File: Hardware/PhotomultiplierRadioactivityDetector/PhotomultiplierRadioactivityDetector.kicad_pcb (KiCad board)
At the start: 2 copper layers, 100 x 100 mm, 128 parts, among them J13 Conn_01x02_Female, J14 Conn_01x04, J15 Conn_02x05_Counter_Clockwise, Q1 2N7002, Q2 Q_NPN_BEC, Q3 Q_NMOS_GDS, U1 TL074, U2 TL074, U3 MCP3425A0T-ECH, U4 LM3488, U5 STM8S003F3P

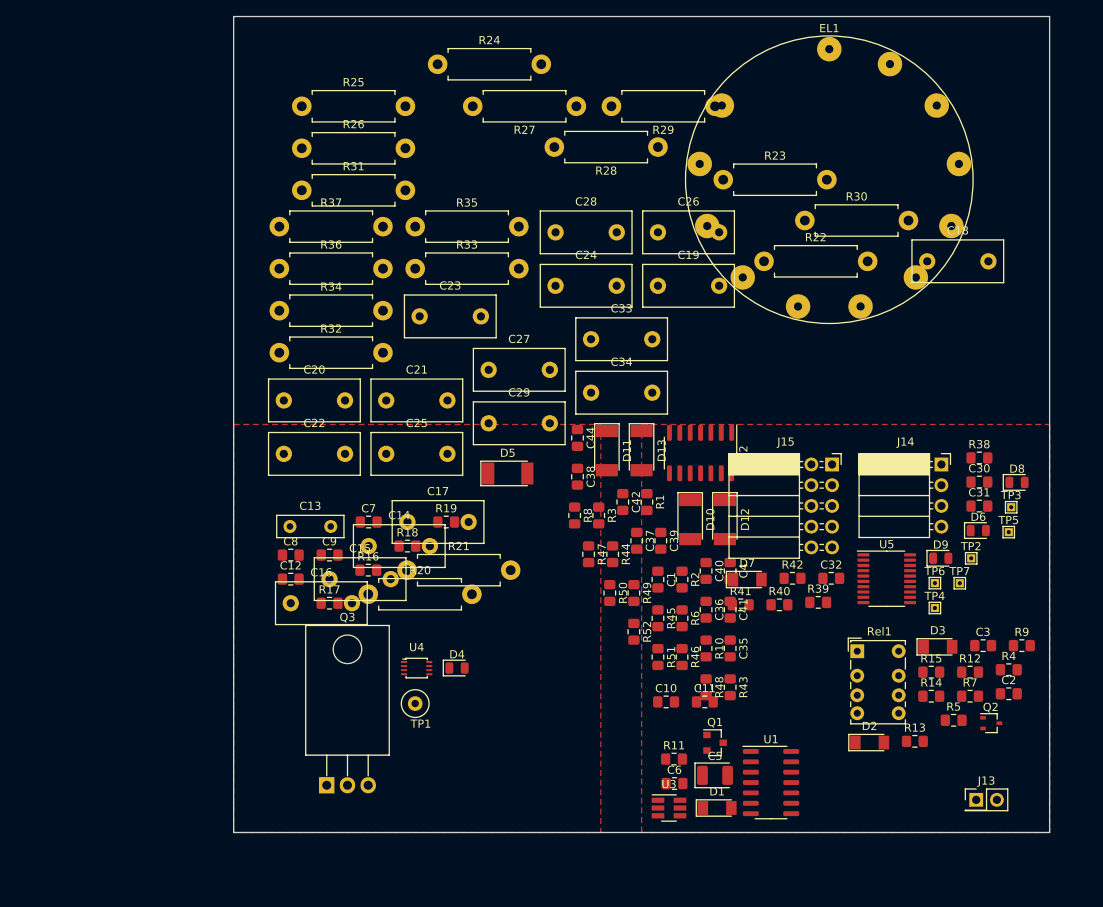
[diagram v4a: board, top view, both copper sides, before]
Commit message: reworked power supply for tube
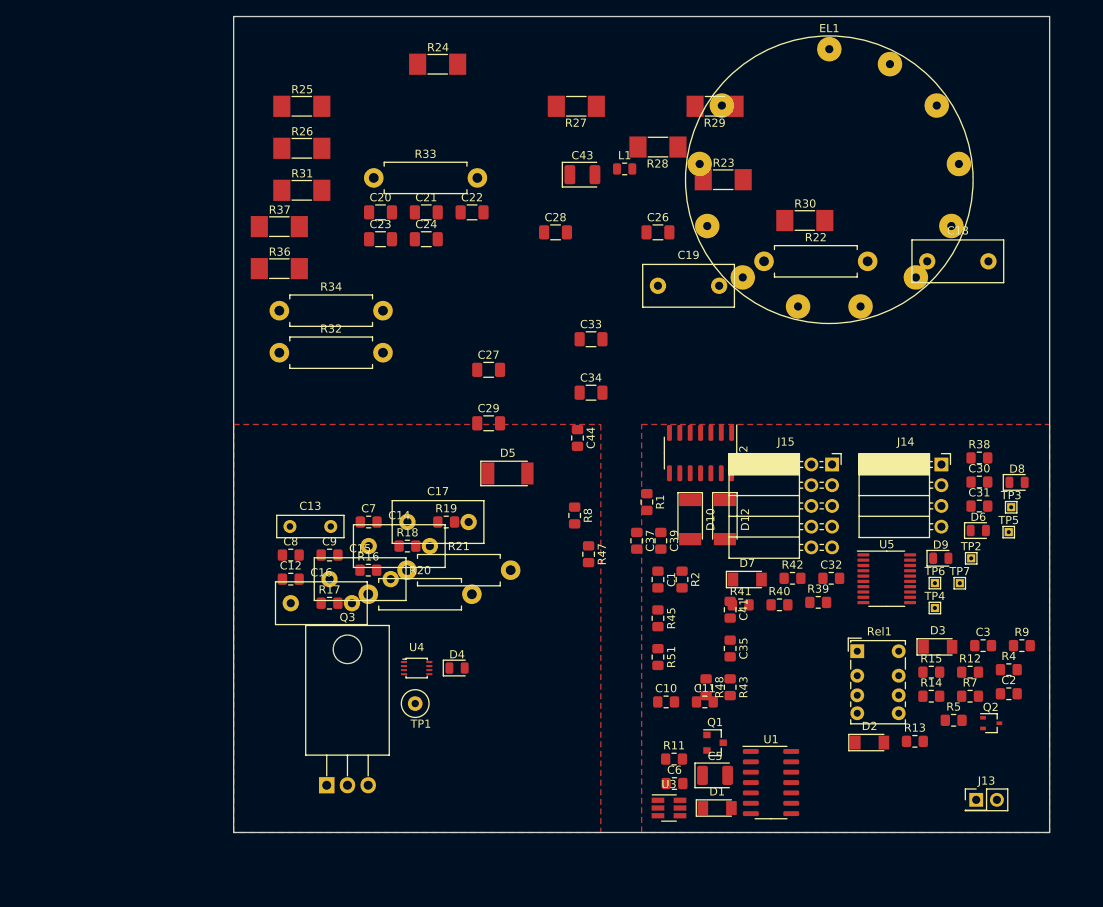
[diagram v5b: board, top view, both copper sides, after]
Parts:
- removed C25: 10n/3kV, Capacitor_THT:C_Disc_D11.0mm_W5.0mm_P7.50mm
- removed C36: 2p2, Capacitor_SMD:C_0805_2012Metric_Pad1.15x1.40mm_HandSolder
- removed C38: 1n, Capacitor_SMD:C_0805_2012Metric_Pad1.15x1.40mm_HandSolder
- removed C4, C40: 100n, Capacitor_SMD:C_0805_2012Metric_Pad1.15x1.40mm_HandSolder
- removed C42: 4p7+2p2, Capacitor_SMD:C_0805_2012Metric_Pad1.15x1.40mm_HandSolder
- removed D11, D13: 1n148, Diode_SMD:D_MELF
- removed R10: 0R, Resistor_SMD:R_0805_2012Metric_Pad1.15x1.40mm_HandSolder
- removed R3, R46, R49, R50, R6: 10k, Resistor_SMD:R_0805_2012Metric_Pad1.15x1.40mm_HandSolder
- removed R35: 150k, Resistor_THT:R_Axial_DIN0411_L9.9mm_D3.6mm_P12.70mm_Horizontal
- removed R44: 10G, Resistor_SMD:R_0805_2012Metric_Pad1.15x1.40mm_HandSolder
- removed R52: 10M, Resistor_SMD:R_0805_2012Metric_Pad1.15x1.40mm_HandSolder
- added C43: 1u/16V, Capacitor_Tantalum_SMD:CP_EIA-3528-21_Kemet-B, F.Cu at (67.7, 109.4)
- added L1: u68, Inductor_SMD:L_0805_2012Metric, F.Cu at (72.9, 108.7)
- C20, C21, C22, C23, C24, C26, C27, C28, C29, C33, C34: footprint Capacitor_THT:C_Disc_D11.0mm_W5.0mm_P7.50mm -> Capacitor_SMD:C_1206_3216Metric
- R23, R24, R25, R26, R27, R28, R31, R36, R37: value 150k -> 1M; footprint Resistor_THT:R_Axial_DIN0411_L9.9mm_D3.6mm_P12.70mm_Horizontal -> Resistor_SMD:R_MELF_MMB-0207
- R29: footprint Resistor_THT:R_Axial_DIN0411_L9.9mm_D3.6mm_P12.70mm_Horizontal -> Resistor_SMD:R_MELF_MMB-0207
- R30: value R -> 1M; footprint Resistor_THT:R_Axial_DIN0411_L9.9mm_D3.6mm_P12.70mm_Horizontal -> Resistor_SMD:R_MELF_MMB-0207
- moved C22 37.5 mm to (54.2, 114.0)
- moved C20 25.9 mm to (43.0, 114.0)
- moved C21 23.6 mm to (48.6, 114.0)
- moved C24 16.8 mm to (48.6, 117.3)
- moved R33 12.2 mm to (42.2, 109.8)
- moved C23 10.6 mm to (43.0, 117.3)
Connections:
- C20 pad 2: DYNOE_OUTPUT -> Net-(C20-Pad2)
- C21 pad 2: Net-(C18-Pad2) -> Net-(C21-Pad2)
- C22 pad 2: Net-(C21-Pad1) -> Net-(C22-Pad2)
- C23 pad 2: Net-(C22-Pad1) -> Net-(C23-Pad2)
- C24 pad 2: Net-(C23-Pad1) -> Net-(C24-Pad2)
- C26 pad 1: Net-(C26-Pad1) -> Net-(C20-Pad2)
- C27 pad 1: Net-(C27-Pad1) -> Net-(C21-Pad2)
- C27 pad 2: Net-(C26-Pad1) -> Net-(C20-Pad1)
- C28 pad 1: Net-(C28-Pad1) -> Net-(C22-Pad2)
- C28 pad 2: Net-(C27-Pad1) -> Net-(C21-Pad1)
- C29 pad 1: Net-(C29-Pad1) -> Net-(C23-Pad2)
- C29 pad 2: Net-(C28-Pad1) -> Net-(C22-Pad1)
- C33 pad 1: Net-(C33-Pad1) -> Net-(C24-Pad2)
- C33 pad 2: Net-(C29-Pad1) -> Net-(C23-Pad1)
- C34 pad 2: Net-(C33-Pad1) -> Net-(C24-Pad1)
- EL1 pad 10: Net-(C33-Pad1) -> Net-(C24-Pad2)
- EL1 pad 11: Net-(EL1-Pad11) -> Net-(C24-Pad1)
- EL1 pad 12: GND -> Net-(EL1-Pad12)
- EL1 pad 2: Net-(C26-Pad1) -> Net-(C20-Pad2)
- EL1 pad 3: Net-(C21-Pad1) -> Net-(C20-Pad1)
- EL1 pad 4: Net-(C27-Pad1) -> Net-(C21-Pad2)
- EL1 pad 5: Net-(C22-Pad1) -> Net-(C21-Pad1)
- EL1 pad 6: Net-(C28-Pad1) -> Net-(C22-Pad2)
- EL1 pad 7: Net-(C23-Pad1) -> Net-(C22-Pad1)
- EL1 pad 8: Net-(C29-Pad1) -> Net-(C23-Pad2)
- EL1 pad 9: Net-(C24-Pad1) -> Net-(C23-Pad1)
- R23 pad 1: Net-(C26-Pad1) -> Net-(C20-Pad2)
- R24 pad 1: Net-(C21-Pad1) -> Net-(C20-Pad1)
- R24 pad 2: Net-(C26-Pad1) -> Net-(C20-Pad2)
- R25 pad 1: Net-(C27-Pad1) -> Net-(C21-Pad2)
- R25 pad 2: Net-(C21-Pad1) -> Net-(C20-Pad1)
- R26 pad 1: Net-(C22-Pad1) -> Net-(C21-Pad1)
- R26 pad 2: Net-(C27-Pad1) -> Net-(C21-Pad2)
- R27 pad 1: Net-(C28-Pad1) -> Net-(C22-Pad2)
- R27 pad 2: Net-(C22-Pad1) -> Net-(C21-Pad1)
- R28 pad 1: Net-(C23-Pad1) -> Net-(C22-Pad1)
- R28 pad 2: Net-(C28-Pad1) -> Net-(C22-Pad2)
- R29 pad 1: Net-(C29-Pad1) -> Net-(C23-Pad2)
- R29 pad 2: Net-(C23-Pad1) -> Net-(C22-Pad1)
- R30 pad 1: Net-(C24-Pad1) -> Net-(C23-Pad1)
- R30 pad 2: Net-(C29-Pad1) -> Net-(C23-Pad2)
- R31 pad 1: Net-(C33-Pad1) -> Net-(C24-Pad2)
- R31 pad 2: Net-(C24-Pad1) -> Net-(C23-Pad1)
- R33 pad 1: DYNOE_OUTPUT -> GND
- R33 pad 2: GND -> Net-(EL1-Pad12)
- R34 pad 1: Net-(C18-Pad2) -> Net-(EL1-Pad12)
- R36 pad 1: Net-(EL1-Pad11) -> Net-(C24-Pad1)
- R36 pad 2: Net-(C33-Pad1) -> Net-(C24-Pad2)
- R37 pad 2: Net-(EL1-Pad11) -> Net-(C24-Pad1)
- U1 pad 10: Net-(C4-Pad1) -> (no net)
- U1 pad 12: Net-(C40-Pad1) -> (no net)
- U1 pad 13: Net-(C42-Pad2) -> (no net)
- U1 pad 14: Net-(C42-Pad1) -> (no net)
- U1 pad 8: Net-(C36-Pad1) -> (no net)
- U1 pad 9: DYNOE_OUTPUT -> (no net)

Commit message: placement of components for tube driver
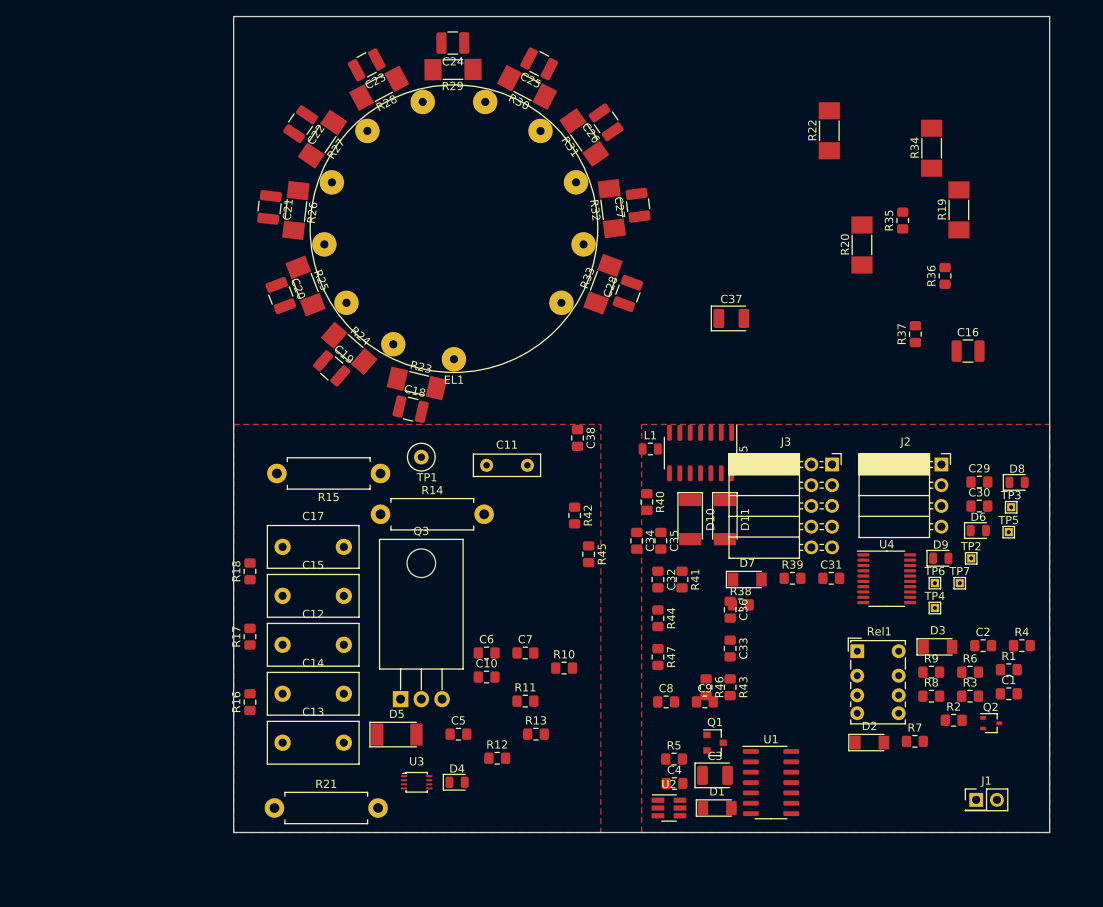
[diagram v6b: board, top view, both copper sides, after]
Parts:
- added R12: 10k, Resistor_SMD:R_0805_2012Metric_Pad1.15x1.40mm_HandSolder, F.Cu at (57.3, 180.9)
- added R16: 1k, Resistor_SMD:R_0805_2012Metric_Pad1.15x1.40mm_HandSolder, F.Cu at (27.0, 174.0)
- added R17: 1k, Resistor_SMD:R_0805_2012Metric_Pad1.15x1.40mm_HandSolder, F.Cu at (27.0, 166.0)
- added R19: 30k, Resistor_SMD:R_MELF_MMB-0207, F.Cu at (113.9, 113.7)
- C12: renamed from C14; value 10n -> 10n/2kV
- C13: renamed from C15; value 10n -> 10n/2kV
- C14: renamed from C16; value 10n -> 10n/2kV
- C15: renamed from C17; value 10n -> 10n/2kV
- C16: renamed from C19; footprint Capacitor_THT:C_Disc_D11.0mm_W5.0mm_P7.50mm -> Capacitor_SMD:C_1210_3225Metric
- C18: renamed from C26; footprint Capacitor_SMD:C_1206_3216Metric -> Capacitor_SMD:C_1210_3225Metric
- C19: renamed from C20; footprint Capacitor_SMD:C_1206_3216Metric -> Capacitor_SMD:C_1210_3225Metric
- C20: renamed from C27; footprint Capacitor_SMD:C_1206_3216Metric -> Capacitor_SMD:C_1210_3225Metric
- C21: footprint Capacitor_SMD:C_1206_3216Metric -> Capacitor_SMD:C_1210_3225Metric
- C22: renamed from C28; footprint Capacitor_SMD:C_1206_3216Metric -> Capacitor_SMD:C_1210_3225Metric
- C23: renamed from C22; footprint Capacitor_SMD:C_1206_3216Metric -> Capacitor_SMD:C_1210_3225Metric
- C24: renamed from C29; footprint Capacitor_SMD:C_1206_3216Metric -> Capacitor_SMD:C_1210_3225Metric
- C25: renamed from C23; footprint Capacitor_SMD:C_1206_3216Metric -> Capacitor_SMD:C_1210_3225Metric
- C26: renamed from C33; footprint Capacitor_SMD:C_1206_3216Metric -> Capacitor_SMD:C_1210_3225Metric
- C27: renamed from C24; footprint Capacitor_SMD:C_1206_3216Metric -> Capacitor_SMD:C_1210_3225Metric
- C28: renamed from C34; footprint Capacitor_SMD:C_1206_3216Metric -> Capacitor_SMD:C_1210_3225Metric
- R18: value 10k -> 1k
- R20: renamed from R32; footprint Resistor_THT:R_Axial_DIN0411_L9.9mm_D3.6mm_P12.70mm_Horizontal -> Resistor_SMD:R_MELF_MMB-0207
- R22: renamed from R34; footprint Resistor_THT:R_Axial_DIN0411_L9.9mm_D3.6mm_P12.70mm_Horizontal -> Resistor_SMD:R_MELF_MMB-0207
- R34: renamed from R33; footprint Resistor_THT:R_Axial_DIN0411_L9.9mm_D3.6mm_P12.70mm_Horizontal -> Resistor_SMD:R_MELF_MMB-0207
- moved R21 89.9 mm to (30.0, 187.0)
- moved C17 86.4 mm to (31.0, 155.0)
- moved R20 72.6 mm to (102.0, 118.0), turned to 90 degrees
- moved R22 70.9 mm to (98.0, 104.0), turned to 90 degrees
- moved R34 68.5 mm to (110.5, 106.1), turned to 90 degrees
- moved C24 46.8 mm to (51.9, 93.3), turned to 180.346 degrees
- moved EL1 46.4 mm to (52.0, 116.0), turned to 180 degrees
- moved R23 45.1 mm to (47.4, 135.0), turned to 346.5 degrees
- moved R36 42.9 mm to (112.2, 121.8), turned to 90 degrees
- moved R32 41.4 mm to (71.3, 113.5), turned to 97.2692 degrees
- moved R33 40.3 mm to (70.3, 122.8), turned to 69.5769 degrees
- moved C16 38.8 mm to (115.0, 131.0)
- moved R30 37.8 mm to (61.0, 98.7), turned to 152.654 degrees
- moved C18 37.3 mm to (46.7, 138.1), turned to 346.5 degrees
- moved R37 37.1 mm to (108.5, 128.9), turned to 90 degrees
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- renumbered C2 to C1, C12 to C10, C13 to C11, C18 to C17, C3 to C2, C30 to C29, C5 to C3, C31 to C30, C32 to C31, C1 to C32, C35 to C33, C37 to C34, C39 to C35, C41 to C36, C43 to C37, C44 to C38, C6 to C4, C7 to C5, C8 to C6, C9 to C7, C10 to C8, C11 to C9, D12 to D11, J13 to J1, J14 to J2, J15 to J3, R4 to R1, R16 to R10, R17 to R11, R19 to R13, R20 to R14, R21 to R15, R5 to R2, R22 to R21, R7 to R3, R36 to R32, R37 to R33, R38 to R35, R39 to R36, R40 to R37, R41 to R38, R42 to R39, R9 to R4, R1 to R40, R2 to R41, R8 to R42, R45 to R44, R47 to R45, R48 to R46, R51 to R47, R11 to R5, R12 to R6, R13 to R7, R14 to R8, R15 to R9, U3 to U2, U4 to U3, U5 to U4, U2 to U5
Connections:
- C12 pad 2: Net-(C14-Pad2) -> Net-(C12-Pad2)
- C13 pad 2: Net-(C14-Pad2) -> Net-(C13-Pad2)
- C15 pad 2: Net-(C14-Pad2) -> Net-(C15-Pad2)
- D5 pad 1: Net-(C14-Pad2) -> Net-(C12-Pad2)
- R14 pad 1: Net-(C14-Pad2) -> Net-(C12-Pad2)
- R18 pad 1: Net-(R18-Pad1) -> Net-(C15-Pad2)
- R18 pad 2: GND -> Net-(C14-Pad2)
- TP1 pad 1: Net-(C14-Pad2) -> Net-(R19-Pad1)
- U3 pad 7: Net-(R18-Pad1) -> Net-(R12-Pad1)

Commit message: add element,, footprint and 3d model for transformer
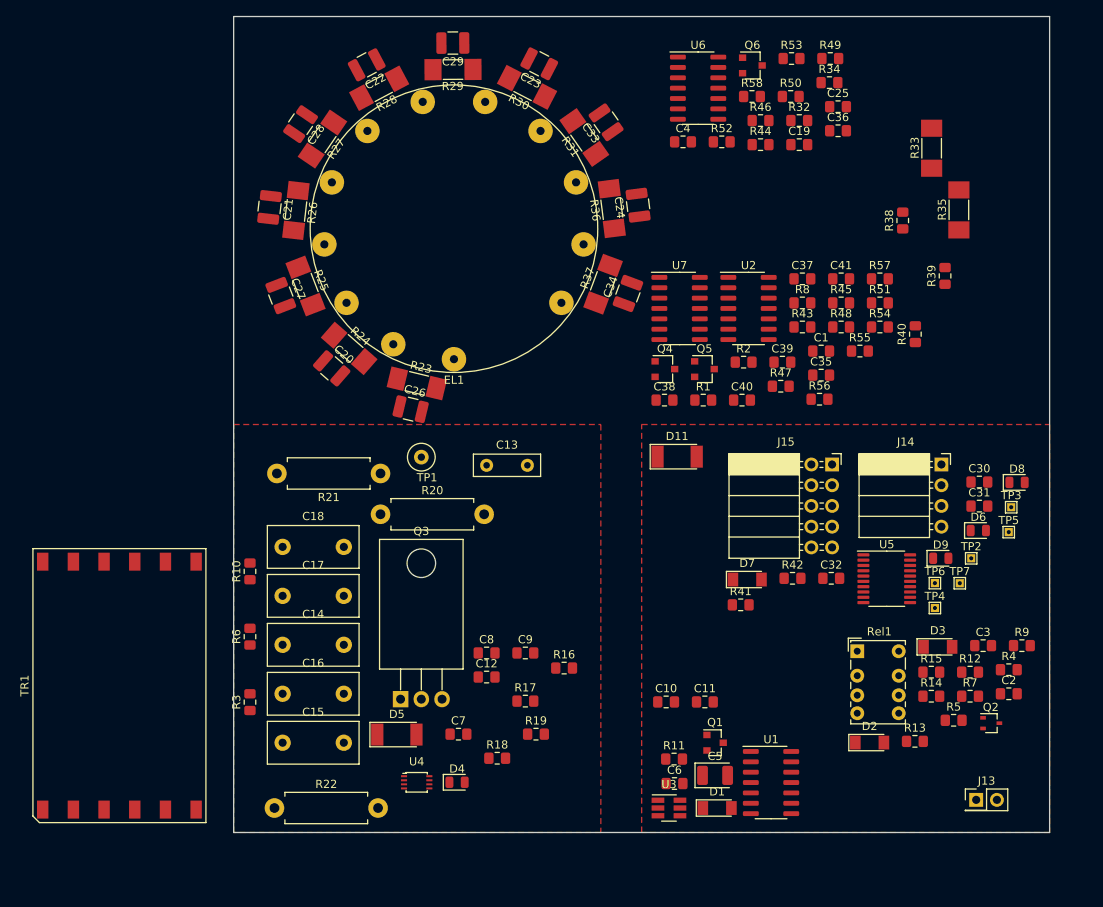
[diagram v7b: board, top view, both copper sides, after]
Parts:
- removed the C16 at (115.0, 131.0)
- removed the C32 at (77.0, 159.0)
- removed the C33 at (85.8, 167.4)
- removed the C34 at (74.4, 154.2)
- removed D10: 1n148, Diode_SMD:D_MELF
- removed L1: u68, Inductor_SMD:L_0805_2012Metric
- removed the R20 at (102.0, 118.0)
- removed the R22 at (98.0, 104.0)
- removed the R40 at (75.6, 149.5)
- removed the R41 at (80.0, 159.0)
- removed the R42 at (66.8, 151.2)
- removed the U5 at (82.2, 143.5)
- added C1: 100n, Capacitor_SMD:C_0805_2012Metric_Pad1.15x1.40mm_HandSolder, F.Cu at (97.0, 131.0)
- added C19: 2p2, Capacitor_SMD:C_0805_2012Metric_Pad1.15x1.40mm_HandSolder, F.Cu at (94.3, 105.7)
- added C25: 100n, Capacitor_SMD:C_0805_2012Metric_Pad1.15x1.40mm_HandSolder, F.Cu at (99.1, 101.0)
- added C39: 1n, Capacitor_SMD:C_0805_2012Metric_Pad1.15x1.40mm_HandSolder, F.Cu at (92.2, 132.4)
- added C4: 100n, Capacitor_SMD:C_0805_2012Metric_Pad1.15x1.40mm_HandSolder, F.Cu at (80.1, 105.4)
- added C40: 100n, Capacitor_SMD:C_0805_2012Metric_Pad1.15x1.40mm_HandSolder, F.Cu at (87.3, 137.0)
- added C41: 4p7+2p2, Capacitor_SMD:C_0805_2012Metric_Pad1.15x1.40mm_HandSolder, F.Cu at (99.5, 122.2)
- added Q4: Q_NJFET_DGS, Package_TO_SOT_SMD:SC-59, F.Cu at (77.8, 133.2)
- added Q5: Q_NJFET_DGS, Package_TO_SOT_SMD:SC-59, F.Cu at (82.7, 133.2)
- added Q6: Q_NJFET_DGS, Package_TO_SOT_SMD:SC-59, F.Cu at (88.6, 96.0)
- added R1: 470k, Resistor_SMD:R_0805_2012Metric_Pad1.15x1.40mm_HandSolder, F.Cu at (82.5, 137.0)
- added R2: 10k, Resistor_SMD:R_0805_2012Metric_Pad1.15x1.40mm_HandSolder, F.Cu at (87.5, 132.4)
- added R32: 10k, Resistor_SMD:R_0805_2012Metric_Pad1.15x1.40mm_HandSolder, F.Cu at (94.3, 102.8)
- added R34: 10k, Resistor_SMD:R_0805_2012Metric_Pad1.15x1.40mm_HandSolder, F.Cu at (98.0, 98.1)
- added R48: 10k, Resistor_SMD:R_0805_2012Metric_Pad1.15x1.40mm_HandSolder, F.Cu at (99.5, 128.1)
- added R49: 10k, Resistor_SMD:R_0805_2012Metric_Pad1.15x1.40mm_HandSolder, F.Cu at (98.1, 95.2)
- added R50: 10k, Resistor_SMD:R_0805_2012Metric_Pad1.15x1.40mm_HandSolder, F.Cu at (93.3, 99.8)
- added R51: 10k, Resistor_SMD:R_0805_2012Metric_Pad1.15x1.40mm_HandSolder, F.Cu at (104.2, 125.1)
- added R52: 10k, Resistor_SMD:R_0805_2012Metric_Pad1.15x1.40mm_HandSolder, F.Cu at (84.8, 105.4)
- added R53: 10M, Resistor_SMD:R_0805_2012Metric_Pad1.15x1.40mm_HandSolder, F.Cu at (93.4, 95.2)
- added R54: 10k, Resistor_SMD:R_0805_2012Metric_Pad1.15x1.40mm_HandSolder, F.Cu at (104.2, 128.1)
- added R55: 10k, Resistor_SMD:R_0805_2012Metric_Pad1.15x1.40mm_HandSolder, F.Cu at (101.8, 131.0)
- added R56: 10k, Resistor_SMD:R_0805_2012Metric_Pad1.15x1.40mm_HandSolder, F.Cu at (96.8, 136.9)
- added R57: 10M, Resistor_SMD:R_0805_2012Metric_Pad1.15x1.40mm_HandSolder, F.Cu at (104.2, 122.2)
- added R58: 10k, Resistor_SMD:R_0805_2012Metric_Pad1.15x1.40mm_HandSolder, F.Cu at (88.5, 99.8)
- added R8: 10k, Resistor_SMD:R_0805_2012Metric_Pad1.15x1.40mm_HandSolder, F.Cu at (94.7, 125.1)
- added TR1: 750311771, PhotomultiplierRadioactivityDetector:750311771, F.Cu at (11.0, 172.0)
- added U2: TL074, Package_SO:SOIC-14_3.9x8.7mm_P1.27mm, F.Cu at (88.1, 125.8)
- added U6: TL074, Package_SO:SOIC-14_3.9x8.7mm_P1.27mm, F.Cu at (81.9, 98.8)
- added U7: TL074, Package_SO:SOIC-14_3.9x8.7mm_P1.27mm, F.Cu at (79.7, 125.8)
- C35: value 100n -> 2p2
- C36: value 4p7+2p2 -> 10n
- C37: value 1u/16V -> 100n; footprint Capacitor_Tantalum_SMD:CP_EIA-3528-21_Kemet-B -> Capacitor_SMD:C_0805_2012Metric_Pad1.15x1.40mm_HandSolder
- R10: renamed from R18; value 1k -> 510R
- R3: renamed from R16; value 1k -> 510R
- R35: renamed from R19; value 30k -> 510R
- R43: value 10G -> 10k
- R44: value 10k -> 0R
- R46: value 10k -> 10G
- R47: value 10M -> 10k
- R6: renamed from R17; value 1k -> 510R
- moved R46 69.8 mm to (89.6, 102.8), turned to 0 degrees
- moved C36 60.2 mm to (99.1, 104.0), turned to 0 degrees
- moved R44 59.4 mm to (89.6, 105.7), turned to 0 degrees
- moved R43 45.0 mm to (94.7, 128.1), turned to 0 degrees
- moved R45 43.7 mm to (99.5, 125.1), turned to 0 degrees
- moved R47 36.4 mm to (92.0, 135.3), turned to 0 degrees
- moved C35 28.3 mm to (97.0, 133.9), turned to 0 degrees
- moved C38 11.6 mm to (77.8, 137.0), turned to 0 degrees
- moved C37 9.96 mm to (94.7, 122.2)
- moved D11 9.68 mm to (79.3, 143.9), turned to 0 degrees
- renumbered C8 to C10, C9 to C11, C10 to C12, C11 to C13, C12 to C14, C13 to C15, C14 to C16, C15 to C17, C17 to C18, C1 to C2, C19 to C20, C23 to C22, C25 to C23, C27 to C24, C18 to C26, C20 to C27, C22 to C28, C24 to C29, C2 to C3, C29 to C30, C30 to C31, C31 to C32, C26 to C33, C28 to C34, C3 to C5, C4 to C6, C5 to C7, C6 to C8, C7 to C9, J1 to J13, J2 to J14, J3 to J15, R5 to R11, R6 to R12, R7 to R13, R8 to R14, R9 to R15, R10 to R16, R11 to R17, R12 to R18, R13 to R19, R14 to R20, R15 to R21, R21 to R22, R34 to R33, R32 to R36, R33 to R37, R35 to R38, R36 to R39, R1 to R4, R37 to R40, R38 to R41, R39 to R42, R2 to R5, R3 to R7, R4 to R9, U2 to U3, U3 to U4, U4 to U5
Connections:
- C35 pad 2: GND -> ANODE_OUTPUT
- C36 pad 1: Net-(C36-Pad1) -> CONTONOUS_MODE_OUTPUT
- C37 pad 1: VCC -> Net-(C37-Pad1)
- EL1 pad 12: Net-(EL1-Pad12) -> ANODE_OUTPUT
- R33 pad 2: Net-(EL1-Pad12) -> ANODE_OUTPUT
- R43 pad 1: Net-(C33-Pad2) -> VCC
- R43 pad 2: Net-(C33-Pad1) -> Net-(C37-Pad1)
- R44 pad 2: Net-(C36-Pad2) -> Net-(C19-Pad2)
- R45 pad 1: VCC -> Net-(C37-Pad1)
- R45 pad 2: Net-(C35-Pad1) -> GND
- R46 pad 1: Net-(C35-Pad1) -> Net-(C19-Pad2)
- R46 pad 2: GND -> Net-(C19-Pad1)
- R47 pad 1: Net-(C36-Pad2) -> Net-(Q5-Pad1)
- R47 pad 2: Net-(C36-Pad1) -> Net-(C38-Pad1)
- U1 pad 11: GND -> (no net)
- U1 pad 4: Net-(C38-Pad1) -> (no net)
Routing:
- added copper zone on F.Cu, net GND
- removed copper zone on F.Cu, net VCC
- removed copper zone on F.Cu, net VCC_5V
